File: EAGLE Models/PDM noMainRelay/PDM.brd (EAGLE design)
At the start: 89.7 x 75.6 mm, 19 parts

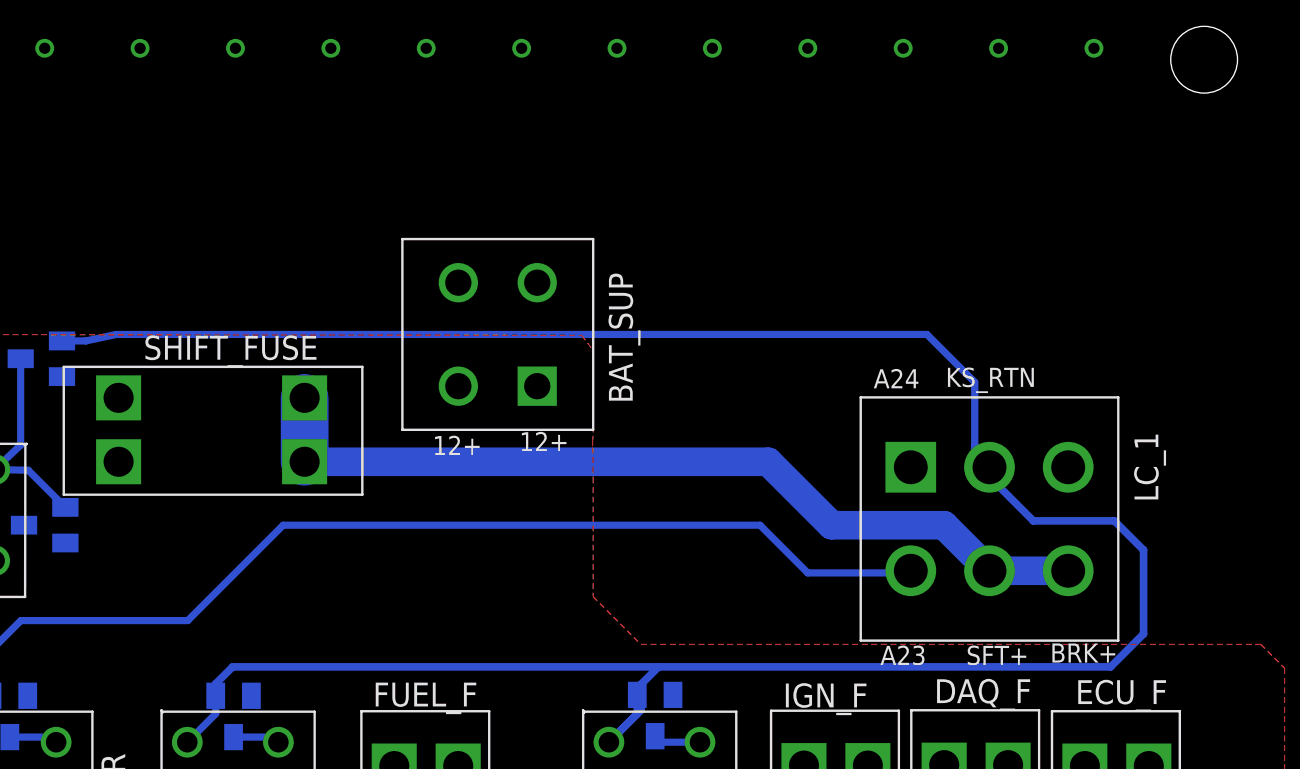
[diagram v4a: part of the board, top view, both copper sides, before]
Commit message: Updated Reverse voltage protection for ecu on PDM
Added Diode
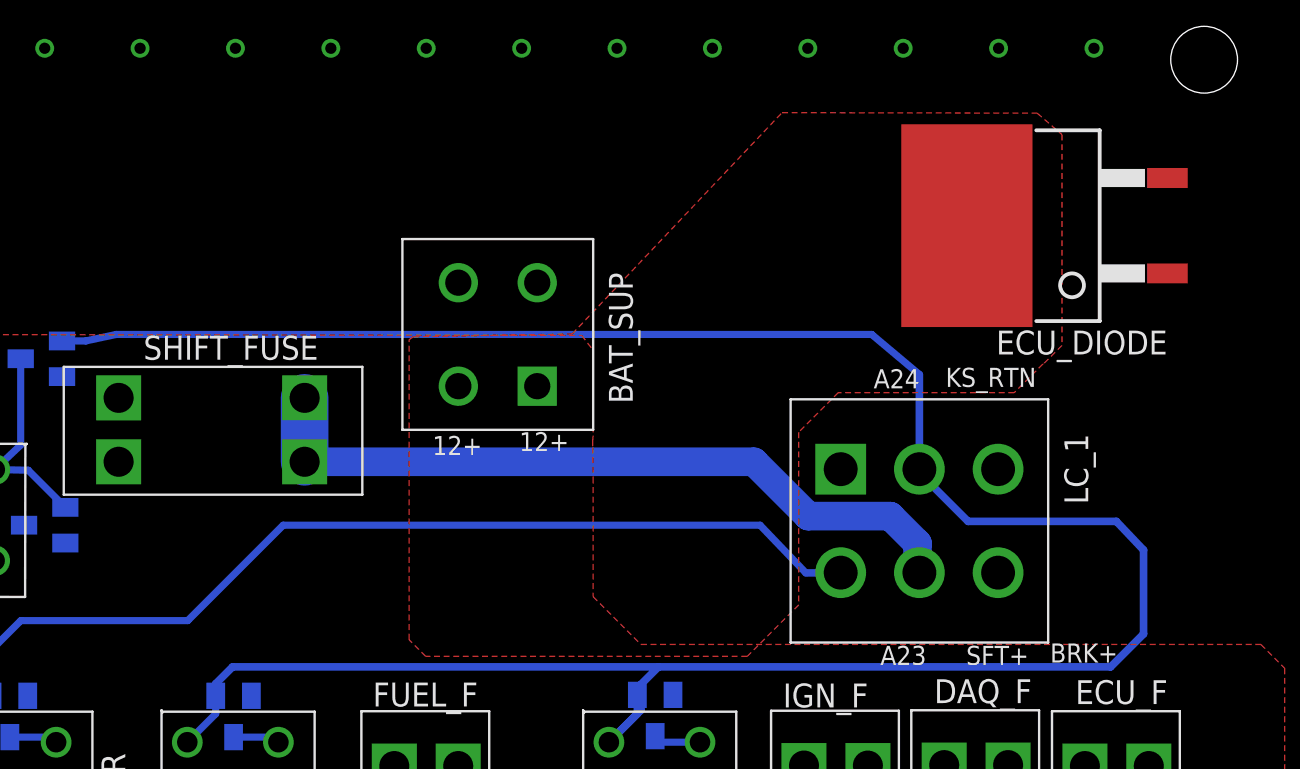
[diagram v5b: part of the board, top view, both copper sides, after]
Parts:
- added ECU_DIODE: VBT2045BP-E3, vishay:TO-263-3
- moved LC_1 3.74 mm to (68.2, 47.2)
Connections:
- net 12V: now also ECU_DIODE.K
- net GND: now also ECU_DIODE.1, ECU_DIODE.2
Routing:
- net 12V_SHIFT_OUT: track 46.6 -> 39.4 mm
- net A23: track 59.3 -> 54.6 mm
- net KILL_SWT_RTRN: track 130.8 -> 132.4 mm
- net 12V: track 8.04 -> 8.66 mm
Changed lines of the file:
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@@
 <layer number="97" name="Info" color="7" fill="1" visible="no" active="no"/>
 <layer number="98" name="Guide" color="6" fill="1" visible="no" active="no"/>
+<layer number="99" name="SpiceOrder" color="5" fill="1" visible="no" active="no"/>
 <layer number="100" name="Muster" color="7" fill="1" visible="no" active="no"/>
 <layer number="101" name="Patch_Top" color="12" fill="4" visible="yes" active="yes"/>
@@
 <attribute name="VALUE" x="69.5452" y="31.4198" size="1.27" layer="27"/>
 </element>
-<element name="LC_1" library="BMS Lbr" package="1586041-6" value="1586041-6" x="71.9074" y="47.3202" smashed="yes">
-<attribute name="NAME" x="80.899" y="48.2092" size="1.27" layer="25" rot="R90"/>
+<element name="LC_1" library="BMS Lbr" package="1586041-6" value="1586041-6" x="68.1736" y="47.2186" smashed="yes">
+<attribute name="NAME" x="77.1652" y="48.1076" size="1.27" layer="25" rot="R90"/>
 </element>
 <element name="LC_2" library="BMS Lbr" package="1586042-8" value="1586042-8" x="55.88" y="8.89" smashed="yes"/>
@@
 <attribute name="NAME" x="25.5778" y="48.3108" size="1.27" layer="26" rot="MR270"/>
 </element>
+<element name="ECU_DIODE" library="vishay" package="TO-263-3" value="VBT2045BP-E3" x="76.3016" y="62.9412" rot="R90"/>
 </elements>
 <signals>
@@
 <contactref element="FAN_D" pad="1"/>
 <wire x1="34.29" y1="46.99" x2="59.69" y2="46.99" width="0.381" layer="16"/>
-<wire x1="59.69" y1="46.99" x2="62.23" y2="44.45" width="0.381" layer="16"/>
-<wire x1="62.23" y1="44.45" x2="67.8307" y2="44.45" width="0.381" layer="16"/>
-<wire x1="68.58" y1="44.45" x2="67.8307" y2="44.45" width="0.381" layer="16"/>
-<wire x1="67.8307" y1="44.45" x2="67.7164" y2="44.5643" width="0.381" layer="16"/>
+<wire x1="59.69" y1="46.99" x2="62.1284" y2="44.45" width="0.381" layer="16"/>
 <wire x1="18.7858" y1="37.9046" x2="18.8112" y2="40.4012" width="0.381" layer="16"/>
 <wire x1="18.8112" y1="40.4012" x2="20.32" y2="41.91" width="0.381" layer="16"/>
@@
 <wire x1="17.3482" y1="35.433" x2="18.7858" y2="36.8706" width="0.381" layer="16"/>
 <wire x1="18.7858" y1="36.8706" x2="18.7858" y2="37.9046" width="0.381" layer="16"/>
+<wire x1="62.1284" y1="44.45" x2="63.9699" y2="44.45" width="0.4064" layer="16"/>
+<wire x1="63.9699" y1="44.45" x2="63.9826" y2="44.4627" width="0.4064" layer="16"/>
 </signal>
 <signal name="IGN_12V">
@@
 <contactref element="SHIFT_FUSE" pad="4"/>
 <wire x1="35.433" y1="50.3682" x2="35.433" y2="53.7718" width="2.54" layer="16"/>
-<wire x1="63.5" y1="46.99" x2="69.4817" y2="46.99" width="1.524" layer="16"/>
-<wire x1="69.4817" y1="46.99" x2="71.9074" y2="44.5643" width="1.524" layer="16"/>
-<wire x1="71.9074" y1="44.5643" x2="76.0857" y2="44.5643" width="1.524" layer="16"/>
-<wire x1="76.0857" y1="44.5643" x2="76.2" y2="44.45" width="1.524" layer="16"/>
-<wire x1="35.433" y1="50.3682" x2="60.1218" y2="50.3682" width="1.524" layer="16"/>
-<wire x1="60.1218" y1="50.3682" x2="63.5" y2="46.99" width="1.524" layer="16"/>
-<wire x1="76.0857" y1="44.5643" x2="76.0984" y2="44.5643" width="0" layer="19" extent="16-16"/>
+<wire x1="35.433" y1="50.3682" x2="59.3598" y2="50.3682" width="1.524" layer="16"/>
+<wire x1="59.3598" y1="50.3682" x2="62.2554" y2="47.4726" width="1.524" layer="16"/>
+<wire x1="62.2554" y1="47.4726" x2="66.6242" y2="47.4726" width="1.524" layer="16"/>
+<wire x1="66.6242" y1="47.4726" x2="68.072" y2="46.0248" width="1.524" layer="16"/>
+<wire x1="68.072" y1="46.0248" x2="68.072" y2="44.5643" width="1.524" layer="16"/>
+<wire x1="68.072" y1="44.5643" x2="68.1736" y2="44.4627" width="1.524" layer="16"/>
+<wire x1="68.1736" y1="44.4627" x2="72.3646" y2="44.4627" width="0" layer="19" extent="1-1"/>
 </signal>
 <signal name="12V_DAQ_OUT">
@@
 <via x="77.47" y="72.39" extent="1-16" drill="0.6"/>
 <contactref element="CC_D" pad="3"/>
+<contactref element="ECU_DIODE" pad="1"/>
+<contactref element="ECU_DIODE" pad="2"/>
 </signal>
 <signal name="12V">
@@
 <vertex x="7.62" y="30.48"/>
 </polygon>
+<wire x1="42.9973" y1="54.3941" x2="43.61941875" y2="54.3941" width="0.4064" layer="1"/>
+<contactref element="ECU_DIODE" pad="K"/>
+<polygon width="0.4064" layer="1">
+<vertex x="41.2242" y="57.023"/>
+<vertex x="49.6824" y="57.1754"/>
+<vertex x="60.8584" y="68.961"/>
+<vertex x="74.4474" y="68.9356"/>
+<vertex x="75.7682" y="67.7926"/>
+<vertex x="75.7682" y="56.5658"/>
+<vertex x="74.7776" y="55.5752"/>
+<vertex x="74.7522" y="55.5752"/>
+<vertex x="73.2282" y="54.0512"/>
+<vertex x="63.8556" y="54.0512"/>
+<vertex x="61.7474" y="51.943"/>
+<vertex x="61.7474" y="42.7482"/>
+<vertex x="59.0042" y="40.005"/>
+<vertex x="41.8846" y="40.005"/>
+<vertex x="40.9956" y="40.894"/>
+<vertex x="40.9956" y="56.8706"/>
+</polygon>
 </signal>
 <signal name="12V_FUSED_ECU">
@@
 <wire x1="22.5122" y1="56.8046" x2="23.7846" y2="56.8046" width="0.381" layer="16"/>
 <wire x1="23.7846" y1="56.8046" x2="25.4" y2="57.15" width="0.381" layer="16"/>
-<wire x1="25.4" y1="57.15" x2="68.58" y2="57.15" width="0.381" layer="16"/>
-<wire x1="68.58" y1="57.15" x2="71.12" y2="54.61" width="0.381" layer="16"/>
-<wire x1="71.12" y1="54.61" x2="71.12" y2="51.2826" width="0.381" layer="16"/>
-<wire x1="71.12" y1="51.2826" x2="71.12" y2="50.8635" width="0.4064" layer="16"/>
+<wire x1="25.4" y1="57.15" x2="65.6336" y2="57.15" width="0.381" layer="16"/>
+<wire x1="65.6336" y1="57.15" x2="68.1736" y2="55.0164" width="0.381" layer="16"/>
 <wire x1="30.6984" y1="38.3184" x2="30.6984" y2="38.547" width="0.4064" layer="16"/>
 <wire x1="30.6984" y1="38.547" x2="31.5976" y2="39.4462" width="0.4064" layer="16"/>
@@
 <wire x1="78.359" y1="39.4462" x2="80.1116" y2="41.1988" width="0.4064" layer="16"/>
 <wire x1="80.1116" y1="41.1988" x2="80.1116" y2="45.6692" width="0.4064" layer="16"/>
-<wire x1="80.1116" y1="45.6692" x2="78.5622" y2="47.2186" width="0.4064" layer="16"/>
-<wire x1="78.5622" y1="47.2186" x2="74.2442" y2="47.2186" width="0.4064" layer="16"/>
-<wire x1="74.2442" y1="47.2186" x2="71.9074" y2="49.5554" width="0.4064" layer="16"/>
-<wire x1="71.9074" y1="49.5554" x2="71.9074" y2="50.0761" width="0.4064" layer="16"/>
+<wire x1="80.1116" y1="45.6692" x2="78.6638" y2="47.1932" width="0.4064" layer="16"/>
+<wire x1="78.6638" y1="47.1932" x2="70.7644" y2="47.1932" width="0.4064" layer="16"/>
 <wire x1="51.6382" y1="35.433" x2="53.152" y2="36.9468" width="0.4064" layer="16"/>
 <wire x1="53.152" y1="36.9468" x2="53.152" y2="37.9554" width="0.4064" layer="16"/>
@@
 <wire x1="53.34" y1="37.1348" x2="53.34" y2="38.5064" width="0.4064" layer="16"/>
 <wire x1="53.34" y1="38.5064" x2="54.2798" y2="39.4462" width="0.4064" layer="16"/>
-<wire x1="71.9074" y1="50.0761" x2="71.12" y2="50.8635" width="0" layer="19" extent="16-16"/>
+<wire x1="68.1736" y1="55.0164" x2="68.1736" y2="49.9745" width="0.4064" layer="16"/>
+<wire x1="68.1736" y1="49.9745" x2="68.1736" y2="49.784" width="0.4064" layer="16"/>
+<wire x1="68.1736" y1="49.784" x2="70.7644" y2="47.1932" width="0.4064" layer="16"/>
 </signal>
 </signals>
